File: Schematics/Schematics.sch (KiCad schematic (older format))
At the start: 8 parts, among them J1 Relay, J2 IR Sensor, J3 BB_I2C, U1 L7805, U2 ATtiny85-20PU

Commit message: The compatibility circuit for the IR Receiver was added to the schematics.
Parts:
- removed J2: IR Sensor, Connector_PinHeader_2.54mm:PinHeader_1x03_P2.54mm_Vertical, symbol Connector_Generic:Conn_01x03
- added C?: 0.1u, Capacitor_THT:C_Disc_D3.0mm_W1.6mm_P2.50mm, symbol Device:C
- added C?: 10u, Capacitor_THT:C_Disc_D3.0mm_W1.6mm_P2.50mm, symbol Device:C
- added J?: IR Sensor, Connector_PinHeader_2.54mm:PinHeader_1x03_P2.54mm_Vertical, symbol Connector_Generic:Conn_01x03
- added R?: 10k, Resistor_THT:R_Axial_DIN0204_L3.6mm_D1.6mm_P1.90mm_Vertical, symbol Device:R
- added R?: 100, Resistor_THT:R_Axial_DIN0204_L3.6mm_D1.6mm_P1.90mm_Vertical, symbol Device:R
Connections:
- wire segments 17 -> 33
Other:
- note added: "IR Circuit"
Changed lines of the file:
@@
 	1    0    0    -1
 $EndComp
-$Comp
-L Connector_Generic:Conn_01x03 J2
-U 1 1 60F91FAD
-P 7700 4150
-F 0 "J2" H 7780 4192 50  0000 L CNN
-F 1 "IR Sensor" H 7780 4101 50  0000 L CNN
-F 2 "Connector_PinHeader_2.54mm:PinHeader_1x03_P2.54mm_Vertical" H 7700 4150 50  0001 C CNN
-F 3 "~" H 7700 4150 50  0001 C CNN
-	1    7700 4150
-	1    0    0    -1
-$EndComp
-$Comp
-L power:VCC #PWR0103
-U 1 1 60F92FA8
-P 7500 4150
-F 0 "#PWR0103" H 7500 4000 50  0001 C CNN
-F 1 "VCC" V 7515 4277 50  0000 L CNN
-F 2 "" H 7500 4150 50  0001 C CNN
-F 3 "" H 7500 4150 50  0001 C CNN
-	1    7500 4150
-	0    -1   -1   0
-$EndComp
-$Comp
-L power:GND #PWR0104
-U 1 1 60F9362D
-P 7500 4250
-F 0 "#PWR0104" H 7500 4000 50  0001 C CNN
-F 1 "GND" V 7505 4122 50  0000 R CNN
-F 2 "" H 7500 4250 50  0001 C CNN
-F 3 "" H 7500 4250 50  0001 C CNN
-	1    7500 4250
-	0    1    1    0
-$EndComp
-Wire Wire Line
-	7500 4050 6150 4050
 Text Label 6950 4050 0    50   ~ 0
 IR_Signal
@@
 Wire Notes Line
 	4400 5900 4400 3300
+Wire Wire Line
+	7500 4050 6150 4050
+$Comp
+L Connector_Generic:Conn_01x03 J?
+U 1 1 6106117F
+P 3900 2250
+F 0 "J?" H 3980 2292 50  0000 L CNN
+F 1 "IR Sensor" H 3980 2201 50  0000 L CNN
+F 2 "Connector_PinHeader_2.54mm:PinHeader_1x03_P2.54mm_Vertical" H 3900 2250 50  0001 C CNN
+F 3 "~" H 3900 2250 50  0001 C CNN
+	1    3900 2250
+	-1   0    0    1
+$EndComp
+$Comp
+L power:VCC #PWR?
+U 1 1 610617CF
+P 5400 1700
+F 0 "#PWR?" H 5400 1550 50  0001 C CNN
+F 1 "VCC" V 5415 1827 50  0000 L CNN
+F 2 "" H 5400 1700 50  0001 C CNN
+F 3 "" H 5400 1700 50  0001 C CNN
+	1    5400 1700
+	1    0    0    -1
+$EndComp
+$Comp
+L power:GND #PWR?
+U 1 1 610624ED
+P 5000 2450
+F 0 "#PWR?" H 5000 2200 50  0001 C CNN
+F 1 "GND" V 5005 2322 50  0000 R CNN
+F 2 "" H 5000 2450 50  0001 C CNN
+F 3 "" H 5000 2450 50  0001 C CNN
+	1    5000 2450
+	0    -1   -1   0
+$EndComp
+$Comp
+L Device:R R?
+U 1 1 61062E0C
+P 5400 1850
+F 0 "R?" H 5330 1804 50  0000 R CNN
+F 1 "10k" H 5330 1895 50  0000 R CNN
+F 2 "Resistor_THT:R_Axial_DIN0204_L3.6mm_D1.6mm_P1.90mm_Vertical" V 5330 1850 50  0001 C CNN
+F 3 "~" H 5400 1850 50  0001 C CNN
+	1    5400 1850
+	-1   0    0    1
+$EndComp
+$Comp
+L Device:R R?
+U 1 1 61063930
+P 5000 1850
+F 0 "R?" H 4930 1804 50  0000 R CNN
+F 1 "100" H 4930 1895 50  0000 R CNN
+F 2 "Resistor_THT:R_Axial_DIN0204_L3.6mm_D1.6mm_P1.90mm_Vertical" V 4930 1850 50  0001 C CNN
+F 3 "~" H 5000 1850 50  0001 C CNN
+	1    5000 1850
+	-1   0    0    1
+$EndComp
+Wire Wire Line
+	5000 1700 5400 1700
+Connection ~ 5400 1700
+Wire Wire Line
+	5000 2000 5000 2150
+Wire Wire Line
+	4100 2250 4300 2250
+Wire Wire Line
+	4300 2250 4300 2450
+Wire Wire Line
+	4300 2450 4550 2450
+Text Label 6000 2350 2    50   ~ 0
+IR_Signal
+$Comp
+L Device:C C?
+U 1 1 6106C3B9
+P 4550 2300
+F 0 "C?" H 4665 2346 50  0000 L CNN
+F 1 "0.1u" H 4665 2255 50  0000 L CNN
+F 2 "Capacitor_THT:C_Disc_D3.0mm_W1.6mm_P2.50mm" H 4588 2150 50  0001 C CNN
+F 3 "~" H 4550 2300 50  0001 C CNN
+	1    4550 2300
+	1    0    0    -1
+$EndComp
+Connection ~ 4550 2150
+Connection ~ 4550 2450
+Wire Wire Line
+	4550 2150 4950 2150
+Wire Wire Line
+	4100 2350 4100 2550
+Wire Wire Line
+	5400 2000 5400 2350
+Wire Wire Line
+	5400 2350 6000 2350
+Connection ~ 5400 2350
+Wire Wire Line
+	5400 2350 5400 2550
+Wire Wire Line
+	4100 2550 5400 2550
+Wire Wire Line
+	4950 2450 5000 2450
+Wire Wire Line
+	4550 2450 4950 2450
+$Comp
+L Device:C C?
+U 1 1 6106CC7A
+P 4950 2300
+F 0 "C?" H 5065 2346 50  0000 L CNN
+F 1 "10u" H 5065 2255 50  0000 L CNN
+F 2 "Capacitor_THT:C_Disc_D3.0mm_W1.6mm_P2.50mm" H 4988 2150 50  0001 C CNN
+F 3 "~" H 4950 2300 50  0001 C CNN
+	1    4950 2300
+	1    0    0    -1
+$EndComp
+Connection ~ 4950 2150
+Wire Wire Line
+	4950 2150 5000 2150
+Connection ~ 4950 2450
+Wire Wire Line
+	4450 2150 4550 2150
+Wire Wire Line
+	4100 2150 4550 2150
+Wire Notes Line
+	3300 1350 3300 2700
+Wire Notes Line
+	3300 2700 6050 2700
+Wire Notes Line
+	6050 2700 6050 1350
+Wire Notes Line
+	3300 1350 6050 1350
+Text Notes 3300 1350 0    50   ~ 0
+IR Circuit
 $EndSCHEMATC

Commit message: The schematic was updated.
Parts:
- gave numbers to parts that had none: 5
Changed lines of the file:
@@
 	4400 5900 4400 3300
 $Comp
-L Connector_Generic:Conn_01x03 J?
+L Connector_Generic:Conn_01x03 J2
 U 1 1 6106117F
 P 3900 2250
-F 0 "J?" H 3980 2292 50  0000 L CNN
+F 0 "J2" H 3980 2292 50  0000 L CNN
 F 1 "IR Sensor" H 3980 2201 50  0000 L CNN
 F 2 "Connector_PinHeader_2.54mm:PinHeader_1x03_P2.54mm_Vertical" H 3900 2250 50  0001 C CNN
@@
 $EndComp
 $Comp
-L power:VCC #PWR?
+L power:VCC #PWR0103
 U 1 1 610617CF
 P 5400 1700
-F 0 "#PWR?" H 5400 1550 50  0001 C CNN
+F 0 "#PWR0103" H 5400 1550 50  0001 C CNN
 F 1 "VCC" V 5415 1827 50  0000 L CNN
 F 2 "" H 5400 1700 50  0001 C CNN
@@
 $EndComp
 $Comp
-L power:GND #PWR?
+L power:GND #PWR0104
 U 1 1 610624ED
 P 5000 2450
-F 0 "#PWR?" H 5000 2200 50  0001 C CNN
+F 0 "#PWR0104" H 5000 2200 50  0001 C CNN
 F 1 "GND" V 5005 2322 50  0000 R CNN
 F 2 "" H 5000 2450 50  0001 C CNN
@@
 $EndComp
 $Comp
-L Device:R R?
+L Device:R R3
 U 1 1 61062E0C
 P 5400 1850
-F 0 "R?" H 5330 1804 50  0000 R CNN
+F 0 "R3" H 5330 1804 50  0000 R CNN
 F 1 "10k" H 5330 1895 50  0000 R CNN
 F 2 "Resistor_THT:R_Axial_DIN0204_L3.6mm_D1.6mm_P1.90mm_Vertical" V 5330 1850 50  0001 C CNN
@@
 $EndComp
 $Comp
-L Device:R R?
+L Device:R R2
 U 1 1 61063930
 P 5000 1850
-F 0 "R?" H 4930 1804 50  0000 R CNN
+F 0 "R2" H 4930 1804 50  0000 R CNN
 F 1 "100" H 4930 1895 50  0000 R CNN
 F 2 "Resistor_THT:R_Axial_DIN0204_L3.6mm_D1.6mm_P1.90mm_Vertical" V 4930 1850 50  0001 C CNN
@@
 IR_Signal
 $Comp
-L Device:C C?
+L Device:C C2
 U 1 1 6106C3B9
 P 4550 2300
-F 0 "C?" H 4665 2346 50  0000 L CNN
+F 0 "C2" H 4665 2346 50  0000 L CNN
 F 1 "0.1u" H 4665 2255 50  0000 L CNN
 F 2 "Capacitor_THT:C_Disc_D3.0mm_W1.6mm_P2.50mm" H 4588 2150 50  0001 C CNN
@@
 	4550 2450 4950 2450
 $Comp
-L Device:C C?
+L Device:C C3
 U 1 1 6106CC7A
 P 4950 2300
-F 0 "C?" H 5065 2346 50  0000 L CNN
+F 0 "C3" H 5065 2346 50  0000 L CNN
 F 1 "10u" H 5065 2255 50  0000 L CNN
 F 2 "Capacitor_THT:C_Disc_D3.0mm_W1.6mm_P2.50mm" H 4988 2150 50  0001 C CNN

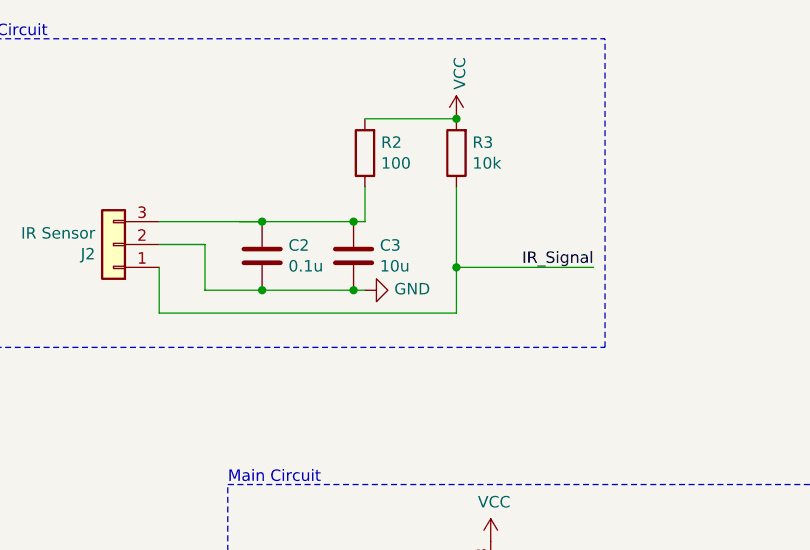
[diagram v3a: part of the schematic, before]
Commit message: A capacitor value was changed.
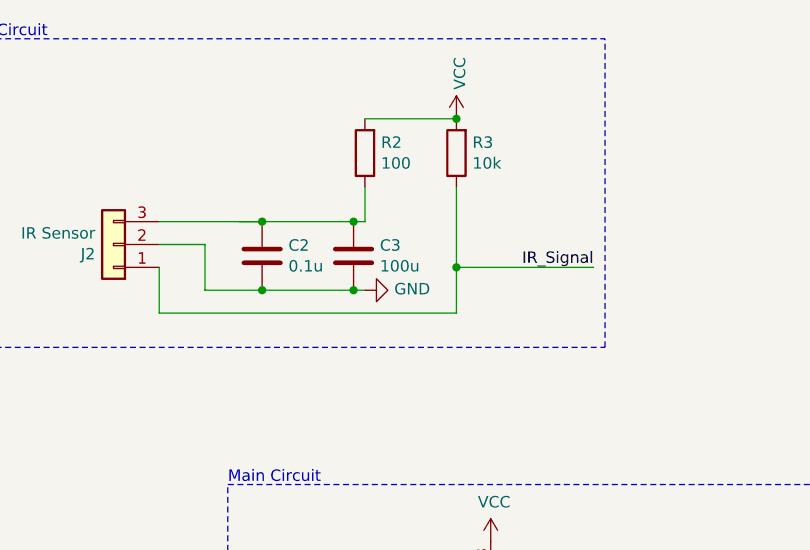
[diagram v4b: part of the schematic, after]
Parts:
- C3: value 10u -> 100u
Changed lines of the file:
@@
 P 4950 2300
 F 0 "C3" H 5065 2346 50  0000 L CNN
-F 1 "10u" H 5065 2255 50  0000 L CNN
+F 1 "100u" H 5065 2255 50  0000 L CNN
 F 2 "Capacitor_THT:C_Disc_D3.0mm_W1.6mm_P2.50mm" H 4988 2150 50  0001 C CNN
 F 3 "~" H 4950 2300 50  0001 C CNN

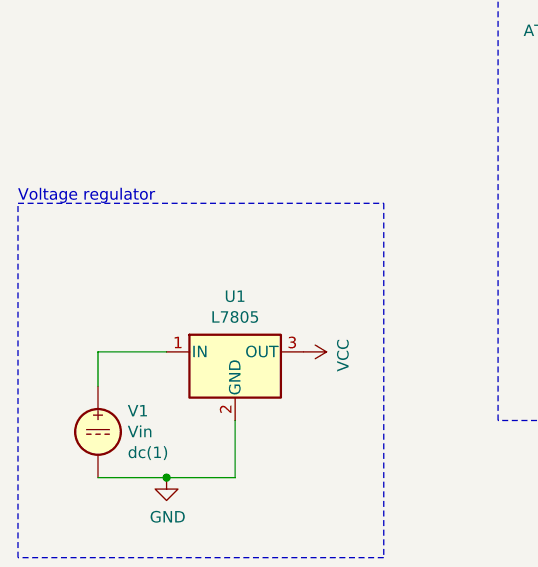
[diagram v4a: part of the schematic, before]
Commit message: A header was removed.
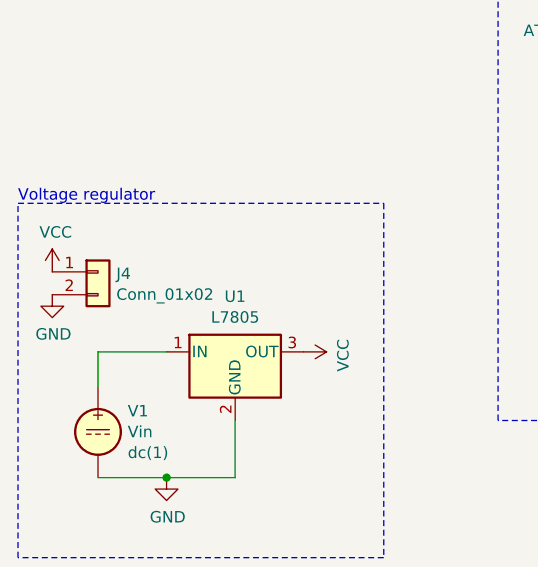
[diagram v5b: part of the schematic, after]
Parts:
- added J4: Conn_01x02, Connector_PinHeader_2.54mm:PinHeader_1x02_P2.54mm_Vertical, symbol Connector_Generic:Conn_01x02
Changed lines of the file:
@@
+	1    0    0    -1
+$EndComp
+$Comp
+L Connector_Generic:Conn_01x02 J4
+U 1 1 61271092
+P 2650 5250
+F 0 "J4" H 2730 5242 50  0000 L CNN
+F 1 "Conn_01x02" H 2730 5151 50  0000 L CNN
+F 2 "Connector_PinHeader_2.54mm:PinHeader_1x02_P2.54mm_Vertical" H 2650 5250 50  0001 C CNN
+F 3 "~" H 2650 5250 50  0001 C CNN
+	1    2650 5250
+	1    0    0    -1
+$EndComp
+$Comp
+L power:VCC #PWR0112
+U 1 1 6127160D
+P 2450 5250
+F 0 "#PWR0112" H 2450 5100 50  0001 C CNN
+F 1 "VCC" H 2465 5423 50  0000 C CNN
+F 2 "" H 2450 5250 50  0001 C CNN
+F 3 "" H 2450 5250 50  0001 C CNN
+	1    2450 5250
+	1    0    0    -1
+$EndComp
+$Comp
+L power:GND #PWR0113
+U 1 1 61271C27
+P 2450 5350
+F 0 "#PWR0113" H 2450 5100 50  0001 C CNN
+F 1 "GND" H 2455 5177 50  0000 C CNN
+F 2 "" H 2450 5350 50  0001 C CNN
+F 3 "" H 2450 5350 50  0001 C CNN
+	1    2450 5350
 	1    0    0    -1
 $EndComp
